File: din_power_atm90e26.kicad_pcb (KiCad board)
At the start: 2 copper layers, 86.9 x 32.8 mm, 60 parts, among them J1 CONN_01X06, J2 VBAT, J3 CONN_01X08, J4 CONN_02X18, J5 CONN_01X08, U1 MCP73831-2-OT, U2 TLV1117-33, U3 TLV1117-33, U4 Hi-Link_SMPS, U5 dc-dc

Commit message: Second iteration
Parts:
- C5, C6, C7, C8, L1, R14, R5, R6, R7: moved to B.Cu
- moved R6 38.5 mm to (117.0, 58.9), turned to 180 degrees
- moved U5 21.2 mm to (132.7, 54.1)
- moved F1 20.8 mm to (124.0, 71.1)
- moved R12 9.35 mm to (127.6, 47.6)
- moved R7 9.27 mm to (117.0, 65.5), turned to 180 degrees
- moved R22 8.88 mm to (149.8, 53.6)
- moved R15 8.80 mm to (142.4, 54.0)
- moved R14 8.40 mm to (116.8, 70.5)
- moved C4 7.87 mm to (162.4, 46.6), turned to 180 degrees
- moved J2 7.29 mm to (148.6, 49.2)
- moved C5 6.96 mm to (144.1, 51.1), turned to 0 degrees
- moved R25 6.85 mm to (154.9, 53.4)
- moved C3 6.83 mm to (153.0, 53.5)
- moved U3 6.79 mm to (141.8, 49.5)
- moved C8 6.63 mm to (140.9, 51.1)
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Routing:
- net +5V_ISO: track 30.3 -> 135.8 mm, vias 1 -> 3
- net /ub_1: track 3.79 -> 55.2 mm, vias 0 -> 1
- net UB: track 47.2 -> 5.23 mm, vias 0 -> 1
- net +3V3: track 50.3 -> 82.7 mm, vias 2 -> 4
- net /ua_2: track 3.10 -> 28.8 mm
- net UN: track 50.4 -> 33.7 mm
- net GNDPWR: track 89.6 -> 76.8 mm, vias 6 -> 5
- net GNDA: track 171.9 -> 182.7 mm, vias 7 -> 8
- net UC: track 34.6 -> 25.9 mm, vias 0 -> 2
- net VBAT: track 35.3 -> 27.2 mm, vias 3 -> 0
- net +5V: track 69.5 -> 61.5 mm, vias 3 -> 5
- net UA_SAMP: track 36.7 -> 28.8 mm, vias 1 -> 5
- net UA: track 13.5 -> 6.43 mm, vias 0 -> 1
- net /uc_2: track 4.16 -> 9.93 mm, vias 0 -> 1
- net +3.3V_ISO: track 57.1 -> 53.8 mm, vias 9 -> 2
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
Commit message: Urbito work 16/11/2017
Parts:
- C1, C2, C3, R12, R13, R15, R16, R17, R22, R23, R24, R25, R26, R27: moved to B.Cu
- L1, U4: moved to F.Cu
- moved C2 26.7 mm to (160.9, 69.1), turned to 0 degrees
- moved R14 25.8 mm to (142.4, 67.1), turned to 180 degrees
- moved R27 25.8 mm to (160.9, 67.2), turned to 180 degrees
- moved R24 25.5 mm to (155.3, 67.1)
- moved R17 25.2 mm to (149.1, 67.1)
- moved R6 22.5 mm to (131.9, 75.8)
- moved R5 20.9 mm to (136.4, 59.6)
- moved C1 19.9 mm to (158.6, 77.4), turned to 0 degrees
- moved R7 19.5 mm to (136.4, 67.1)
- moved R12 19.2 mm to (142.6, 59.6)
- moved R26 18.2 mm to (158.6, 75.8), turned to 180 degrees
- moved R13 17.9 mm to (138.6, 75.8), turned to 180 degrees
- moved C3 11.2 mm to (161.8, 60.3), turned to 270 degrees
- moved R15 8.63 mm to (148.9, 59.6)
- moved R25 8.29 mm to (159.4, 60.3), turned to 90 degrees
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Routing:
- net +5V_ISO: track 135.8 -> 50.3 mm, vias 3 -> 4
- net /ub_1: track 55.2 -> 3.82 mm, vias 1 -> 0
- net +3V3: track 82.7 -> 44.2 mm, vias 4 -> 5
- net UA: track 6.43 -> 33.6 mm
- net UC_SAMP: track 38.4 -> 11.6 mm, vias 1 -> 0
- net UB: track 5.23 -> 31.3 mm, vias 1 -> 3
- net /ua_2: track 28.8 -> 3.44 mm
- net GNDA: track 182.7 -> 159.4 mm
- net +5V: track 61.5 -> 79.1 mm, vias 5 -> 9
- net UB_SAMP: track 34.9 -> 19.3 mm, vias 1 -> 2
- net UA_SAMP: track 28.8 -> 15.4 mm, vias 5 -> 2
- net /ua_1: track 13.0 -> 3.30 mm, vias 1 -> 0
- net GNDPWR: track 76.8 -> 68.4 mm, vias 5 -> 4
- net UC: track 25.9 -> 32.6 mm
- net UN: track 33.7 -> 40.3 mm, vias 3 -> 0
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
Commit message: Urbito work 17/11/2017
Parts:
- moved C9 9.84 mm to (163.8, 49.3), turned to 270 degrees
- moved R22 9.24 mm to (146.4, 57.1)
- moved R15 8.98 mm to (140.3, 57.2)
- moved R32 8.82 mm to (163.4, 46.6)
- moved R5 8.77 mm to (128.0, 57.1)
- moved R12 8.76 mm to (134.2, 57.1)
- moved C7 8.65 mm to (141.8, 50.8)
- moved U2 8.65 mm to (142.6, 49.3)
- moved C6 8.65 mm to (145.0, 50.9)
- moved R33 7.85 mm to (170.2, 48.3)
- moved C8 7.84 mm to (148.5, 52.9)
- moved D1 7.77 mm to (166.4, 48.6), turned to 180 degrees
- moved C5 7.66 mm to (151.5, 52.9)
- moved U3 7.49 mm to (149.3, 49.1)
- moved J2 6.60 mm to (155.2, 48.8)
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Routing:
- net +3V3: track 44.2 -> 30.3 mm, vias 5 -> 1
- net UA_SAMP: track 15.4 -> 28.6 mm, vias 2 -> 3
- net GNDPWR: track 68.4 -> 57.2 mm
- net UC: track 32.6 -> 42.4 mm, vias 2 -> 0
- net +3.3V_ISO: track 58.4 -> 49.0 mm, vias 2 -> 3
- net +5V: track 79.1 -> 85.0 mm
- net VBAT: track 27.4 -> 22.6 mm, vias 1 -> 2
- net Net-(D2-Pad1): track 6.12 -> 1.74 mm, vias 1 -> 0
- net GNDA: track 159.4 -> 155.3 mm, vias 8 -> 7
- net UA: track 33.6 -> 30.1 mm, vias 1 -> 0
- net /UN_IN: track 7.58 -> 10.5 mm
- net +5V_ISO: track 50.3 -> 52.9 mm, vias 4 -> 1
- net UB: track 31.3 -> 33.4 mm, vias 3 -> 1
- net UB_SAMP: track 19.3 -> 20.8 mm, vias 2 -> 1
- net Net-(R32-Pad1): track 4.61 -> 5.51 mm
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
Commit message: Urbito delivery 18/11/2017
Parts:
- C5, C8, R10, R11, R20, R21, R3, R30, R31, R4: moved to F.Cu
- moved R4 13.2 mm to (174.8, 46.4), turned to 180 degrees
- moved R30 12.9 mm to (174.8, 76.4), turned to 0 degrees
- moved R11 11.9 mm to (174.8, 61.5), turned to 180 degrees
- moved R3 11.7 mm to (174.8, 48.3), turned to 0 degrees
- moved R31 11.3 mm to (174.8, 74.5), turned to 180 degrees
- moved R20 7.52 mm to (179.1, 61.5), turned to 0 degrees
- moved R10 6.81 mm to (182.5, 61.4), turned to 0 degrees
- moved R21 5.91 mm to (186.0, 61.4)
- moved C8 0.85 mm to (148.5, 52.1)
- moved C5 0.81 mm to (151.5, 52.1)
- moved U3 0.29 mm to (149.3, 48.9)
- moved R28 0.17 mm to (174.8, 69.8)
- moved R29 0.16 mm to (174.8, 72.3)
- moved R19 0.15 mm to (174.8, 67.3)
- moved R8 0.14 mm to (174.8, 55.7)
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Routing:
- net IB1+: track 24.4 -> 93.6 mm, vias 1 -> 4
- net IB2+: track 89.3 -> 22.0 mm
- net IA1+: track 33.3 -> 86.4 mm, vias 1 -> 4
- net IB1-: track 55.9 -> 103.8 mm, vias 1 -> 3
- net IC1+: track 33.3 -> 74.4 mm, vias 0 -> 4
- net IC2-: track 50.7 -> 82.9 mm, vias 1 -> 2
- net IC1-: track 64.7 -> 81.3 mm, vias 2 -> 0
- net GNDA: track 155.3 -> 139.8 mm, vias 7 -> 8
- net IB2-: track 72.9 -> 88.2 mm, vias 0 -> 2
- net IA2+: track 17.2 -> 9.50 mm, vias 2 -> 1
- net IN2-: track 53.6 -> 46.3 mm
- net IN1+: track 22.5 -> 19.3 mm, vias 2 -> 1
- net IA2-: track 20.3 -> 17.4 mm, vias 3 -> 1
- net IN2+: track 49.5 -> 47.5 mm, vias 2 -> 0
- net IC2+: track 17.2 -> 18.8 mm, vias 1 -> 2
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
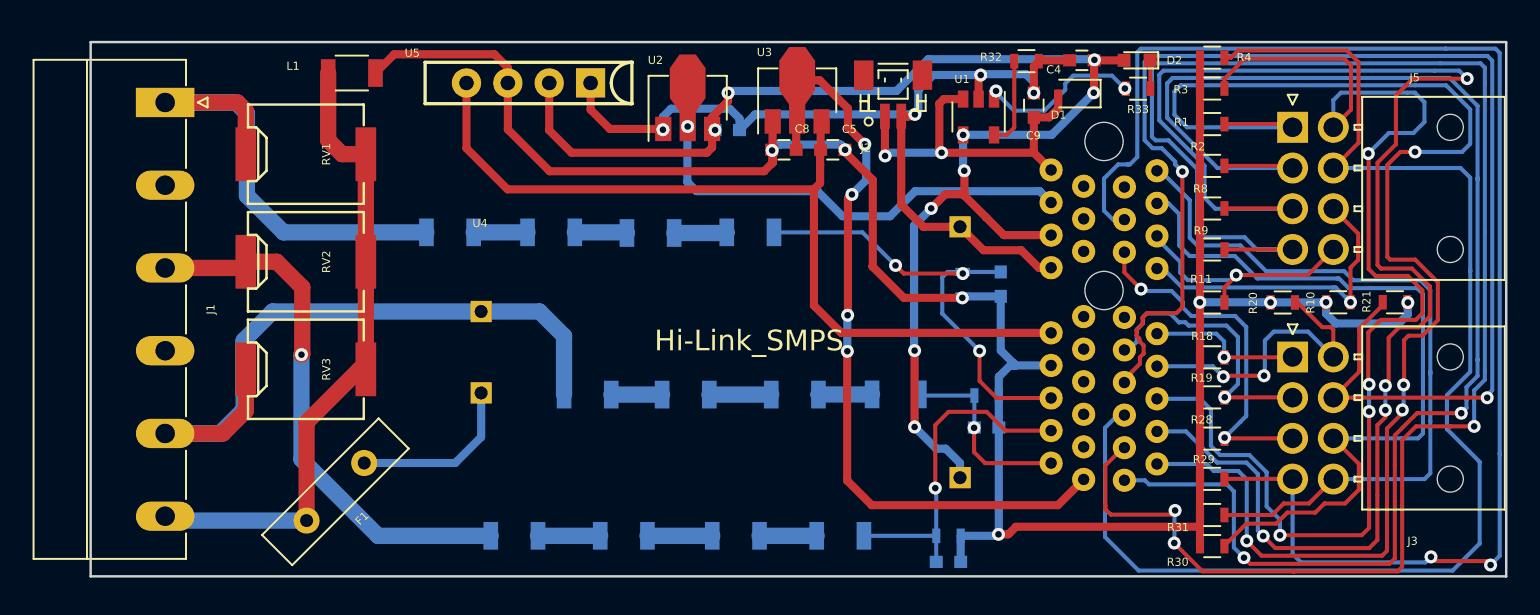
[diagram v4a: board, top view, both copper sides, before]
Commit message: Reroute sections, clean up silk screen
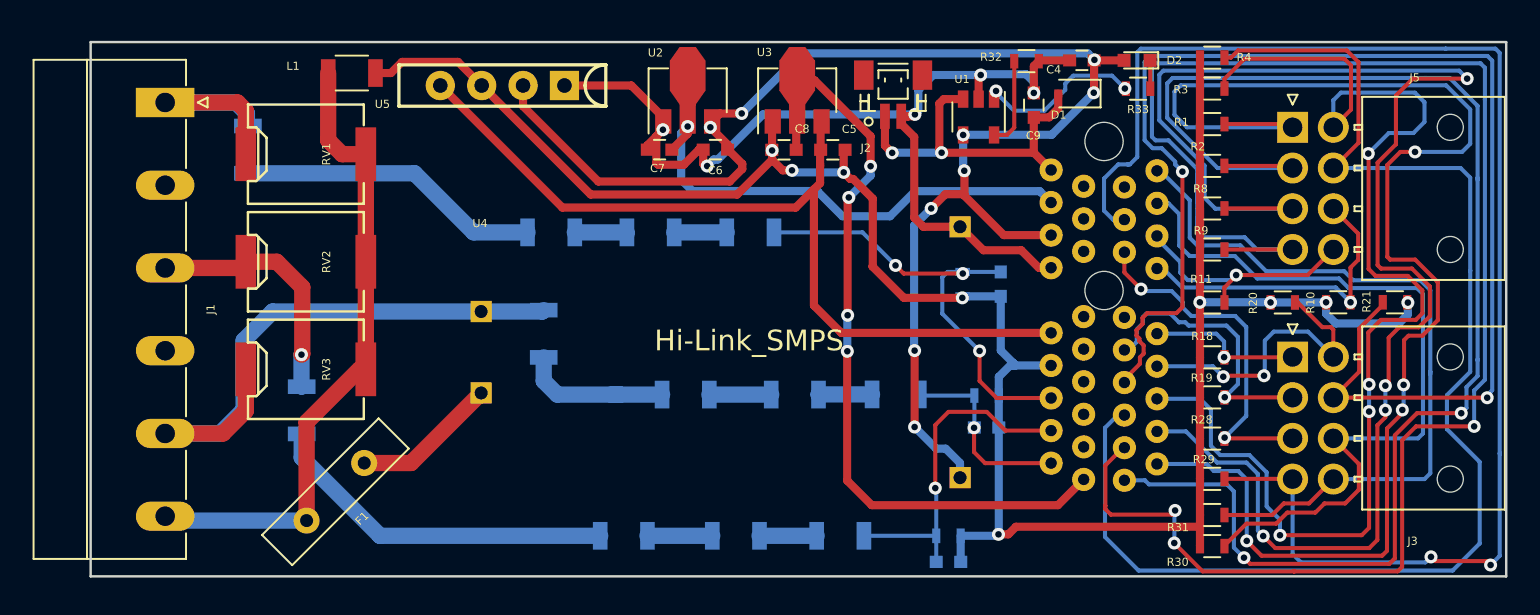
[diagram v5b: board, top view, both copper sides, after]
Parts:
- C6, C7: moved to F.Cu
- moved R6 15.2 mm to (118.9, 68.1), turned to 90 degrees
- moved R5 13.4 mm to (115.6, 52.1), turned to 90 degrees
- moved R7 4.61 mm to (133.7, 63.4), turned to 90 degrees
- moved U5 1.61 mm to (131.2, 48.1)
- moved C7 1.55 mm to (140.8, 52.1)
- moved C6 1.40 mm to (144.3, 52.1), turned to 180 degrees
- moved U2 0.46 mm to (142.6, 48.9)
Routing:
- net UB: track 33.4 -> 15.4 mm
- net /ub_1: track 3.82 -> 21.8 mm
- net UA: track 30.1 -> 13.9 mm
- net /ua_1: track 3.31 -> 18.7 mm
- net /uc_1: track 3.12 -> 9.61 mm
- net GNDPWR: track 57.2 -> 63.0 mm, vias 4 -> 5
- net +5V: track 85.0 -> 90.4 mm
- net UC: track 42.4 -> 36.9 mm
- net +3V3: track 31.6 -> 35.4 mm
- net GNDA: track 139.8 -> 137.6 mm, vias 8 -> 9
- net /UN_IN: track 10.5 -> 8.96 mm
- net VBAT: track 22.6 -> 22.1 mm

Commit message: Add OSHW logo
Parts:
- added LOGO_OSHW1: Logo_Open_Hardware_Small, Symbols:OSHW-Symbol_6.7x6mm_SilkScreen, B.Cu at (188.2, 54.5)
- moved G1 36.8 mm to (187.7, 68.6), turned to 90 degrees
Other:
- board text added: "TAPR"
- board text added: "Whatnick Emon Base v1.1 18/11/2017"
- board text removed: "Whatnick Emon Base v1.0 04/11/2017"
